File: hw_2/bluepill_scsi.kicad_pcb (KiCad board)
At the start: 2 copper layers, 26.9 x 72.2 mm, 94 parts, among them J1 Conn_02x02_Odd_Even, J2 Conn_01x04_Male, J3 USB_B_Micro, J4 Berg Power Connector, J5 Conn_02x25_Odd_Even, J6 Micro_SD_Card, J8 Conn_01x04_Male, SW1 SW_Push, U1 MIC5504-3.3YM5, U2 STM32F103C8Tx, Y2 8MHz, Y3 32.768k

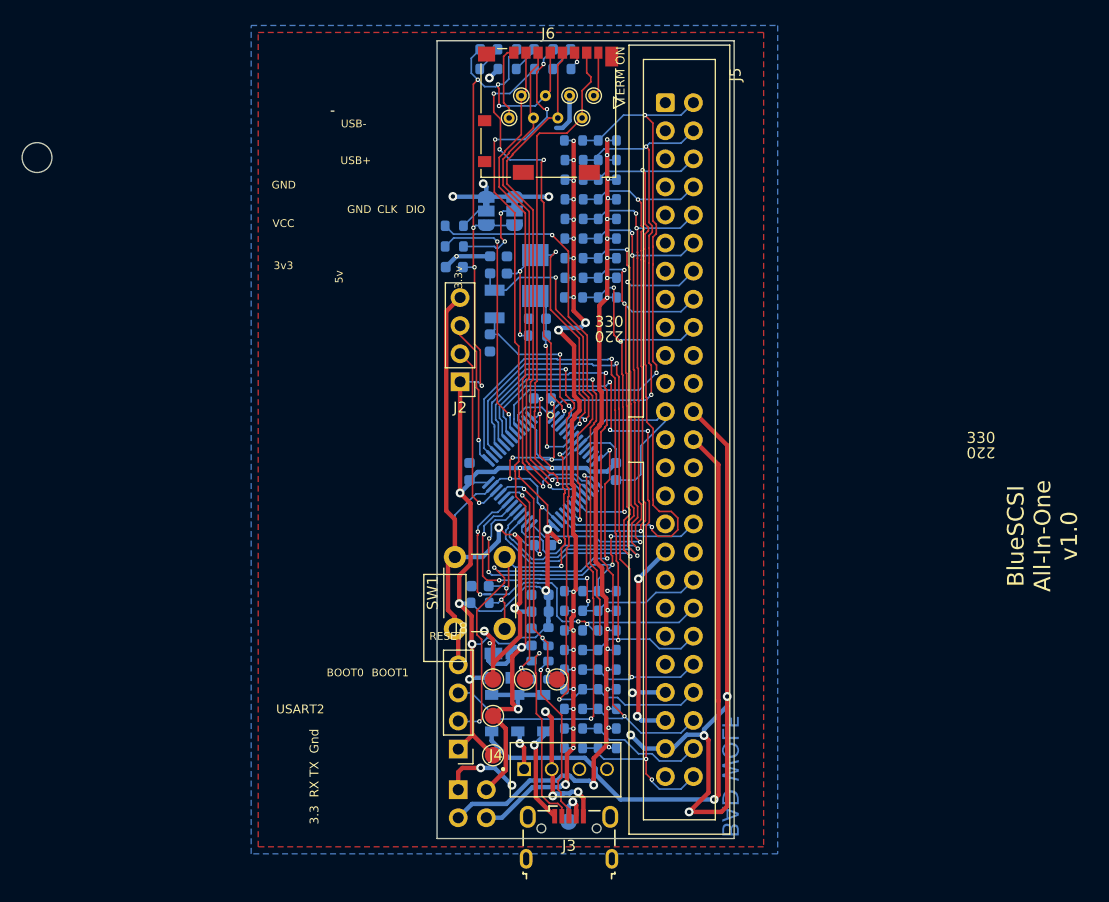
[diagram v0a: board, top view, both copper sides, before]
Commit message: Updated silkscreens
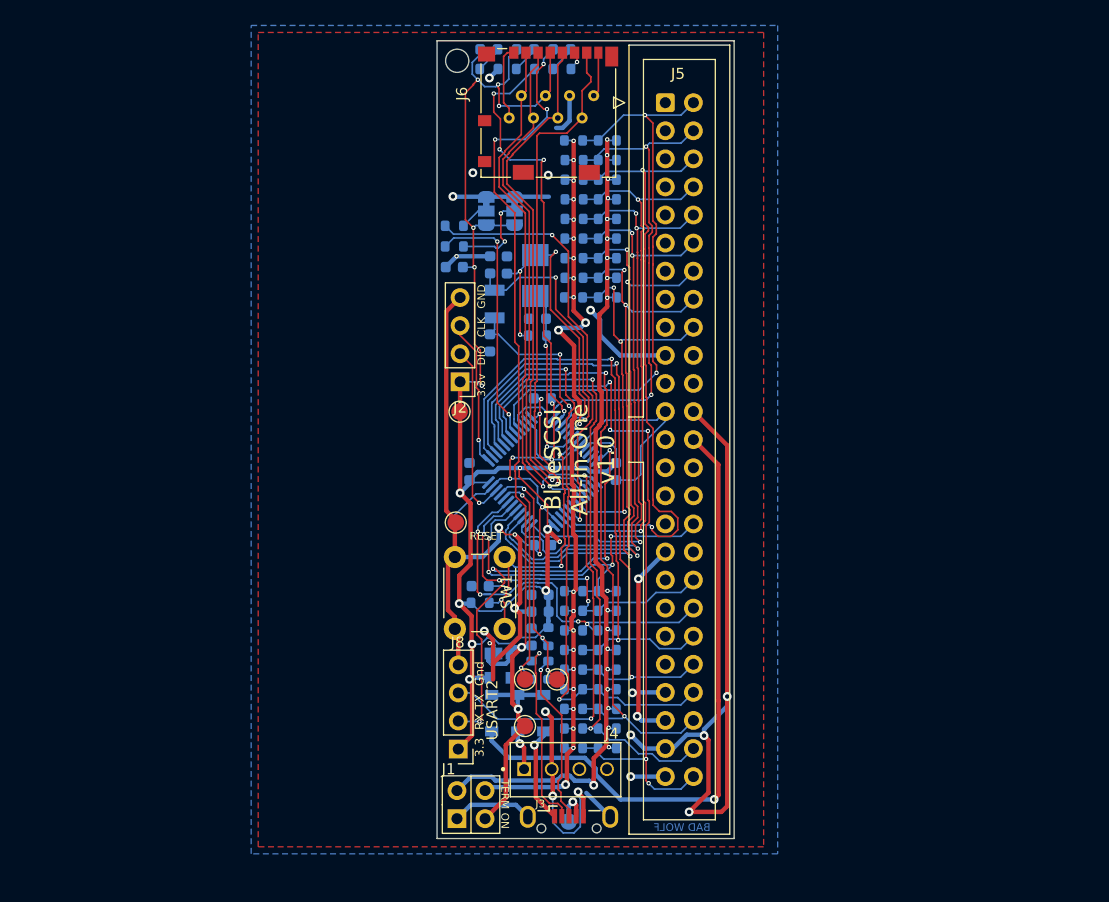
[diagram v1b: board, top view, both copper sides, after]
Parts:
- removed H1: MountingHole_Pad, MountingHole:MountingHole_2.7mm_M2.5
- added REF**: MountingHole_2.1mm, MountingHole:MountingHole_2.1mm, F.Cu at (88.5, 78.1)
- J1: moved to F.Cu
- TP12, TP13, TP7, TP8, TP9: moved to B.Cu
- moved TP4 31.2 mm to (88.7, 109.9)
- moved TP14 14.6 mm to (88.4, 119.9)
- moved TP5 3.03 mm to (94.6, 138.3)
- moved J1 2.63 mm to (88.5, 146.7), turned to 90 degrees
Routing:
- net GND: track 248.7 -> 269.3 mm
- net SCSI_REQ: track 48.4 -> 57.2 mm, vias 1 -> 2
- net +3V3: track 161.8 -> 159.6 mm
- net VCC: track 88.7 -> 90.0 mm
- net Net-(J1-Pad4): track 85.8 -> 84.9 mm
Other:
- board text added: "0"
- board text added: "1"
- board text added: "Boot Sel"
- board text added: "MSIO"
- board text removed: "5v"
- board text removed: "BOOT0"
- board text removed: "BOOT1"
- board text removed: "Boot 0"
- board text removed: "Boot 1"
- board text removed: "DBG"
- board text removed: "MISO"
- board text removed: "PC13"
- board text removed: "USB+"
- board text removed: "USB-"
- board text removed: "VCC"

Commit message: Version 1.0 as ordered
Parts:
- added G***: LOGO, SamacSys_Parts:dogcow, F.Cu at (99.7, 127.1)
- added G***: LOGO, SamacSys_Parts:mac_happy_small, F.Cu at (100.5, 103.8)
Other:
- board text added: "Berg Power"
- board text added: "CC"
- board text added: "CC BY-NC"
- board text added: "JLCJLCJLCJLC"
- board text added: "PROGRAMMING"
- board text added: "http://scsi.blue"
